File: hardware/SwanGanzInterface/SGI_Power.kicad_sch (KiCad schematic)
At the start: 23 parts, among them IC2 LM2937ET-3.3_NOPB, IC3 LM4041CILPR, J1 2479774-1, Q1 SQ2389CES-T1_GE3, SW1 Power_Switch, U3 OPA2350

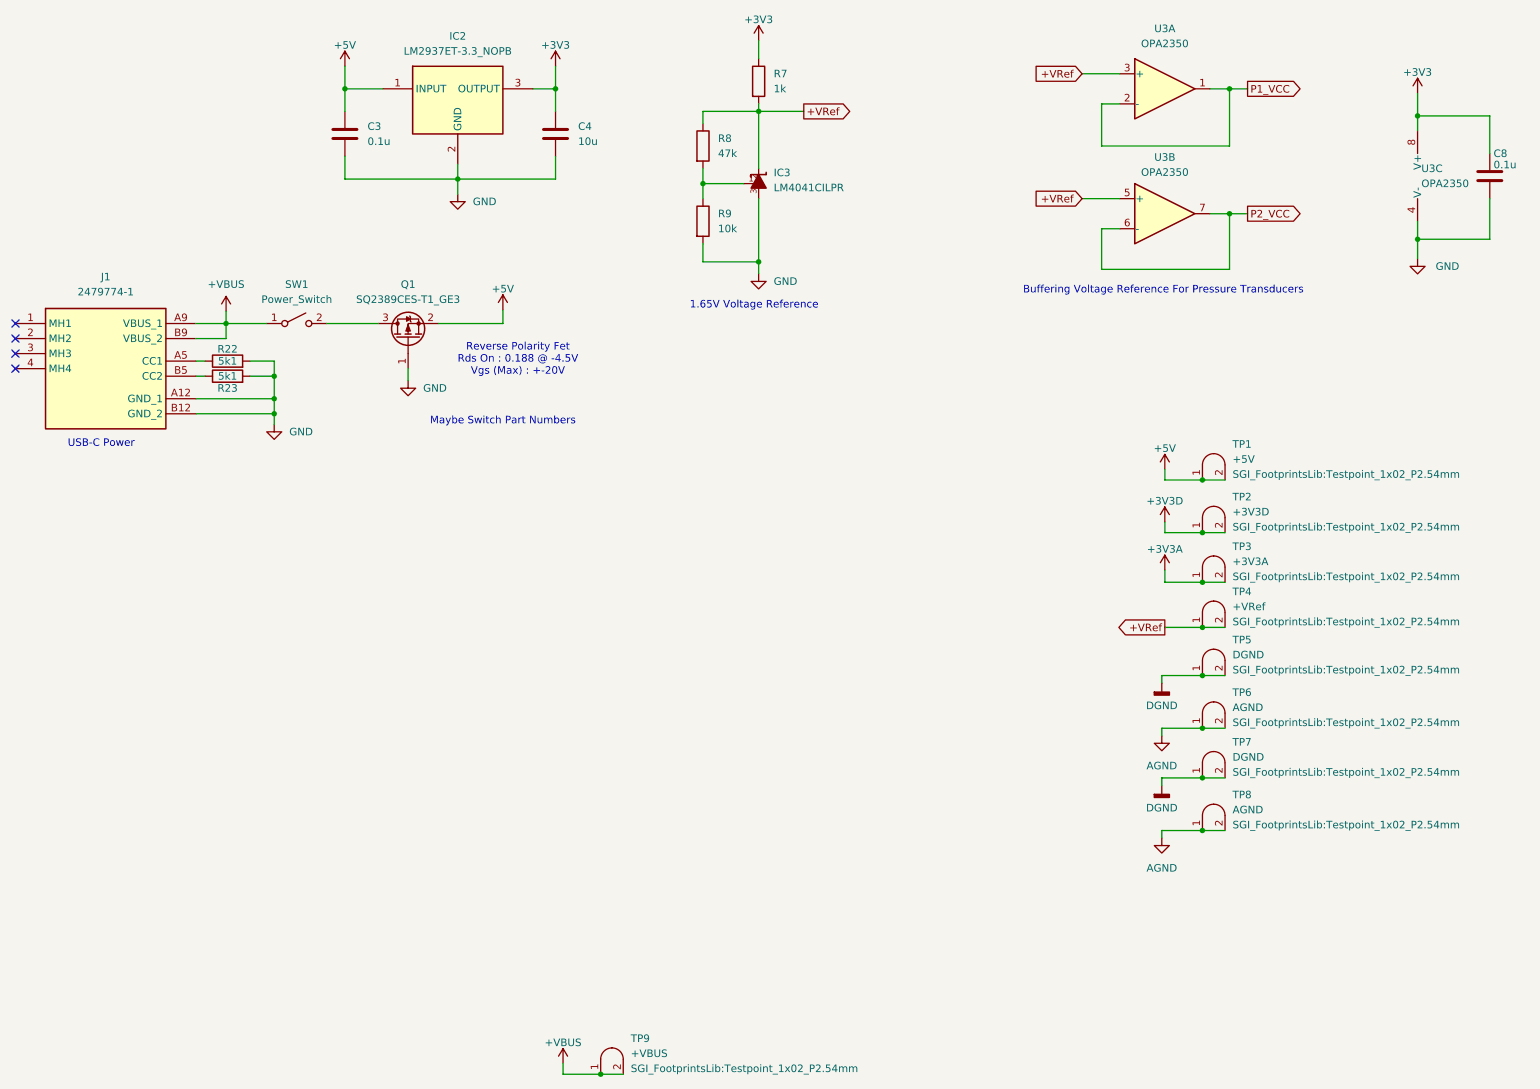
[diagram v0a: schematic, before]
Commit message: Added launchpad, power jumpers, messed with symbol lib
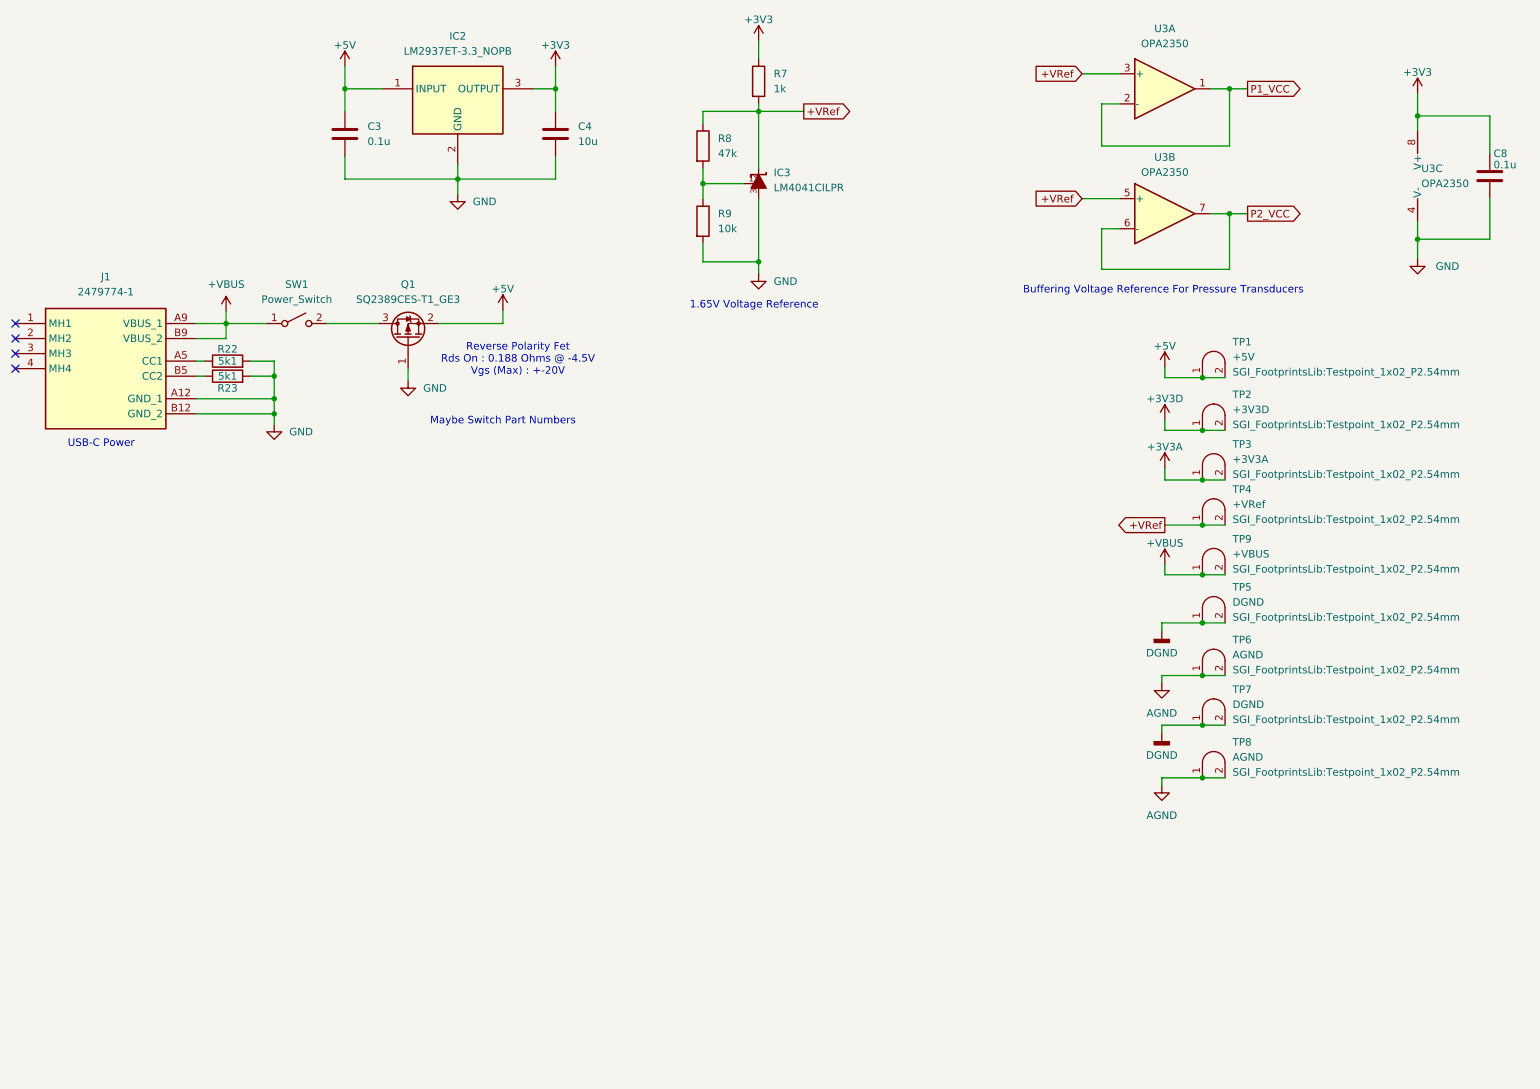
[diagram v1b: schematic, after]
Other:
- note added: "Reverse Polarity Fet Rds On : 0.188 Ohms @ -4.5V Vgs (Max) : +-20V"
- note removed: "Reverse Polarity Fet Rds On : 0.188 @ -4.5V Vgs (Max) : +-20V"
- moved on the sheet: TP1, TP2, TP3, TP4, TP5, TP6, TP7, TP8, TP9

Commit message: Added Test Points to the Outputs of Analog Circuits
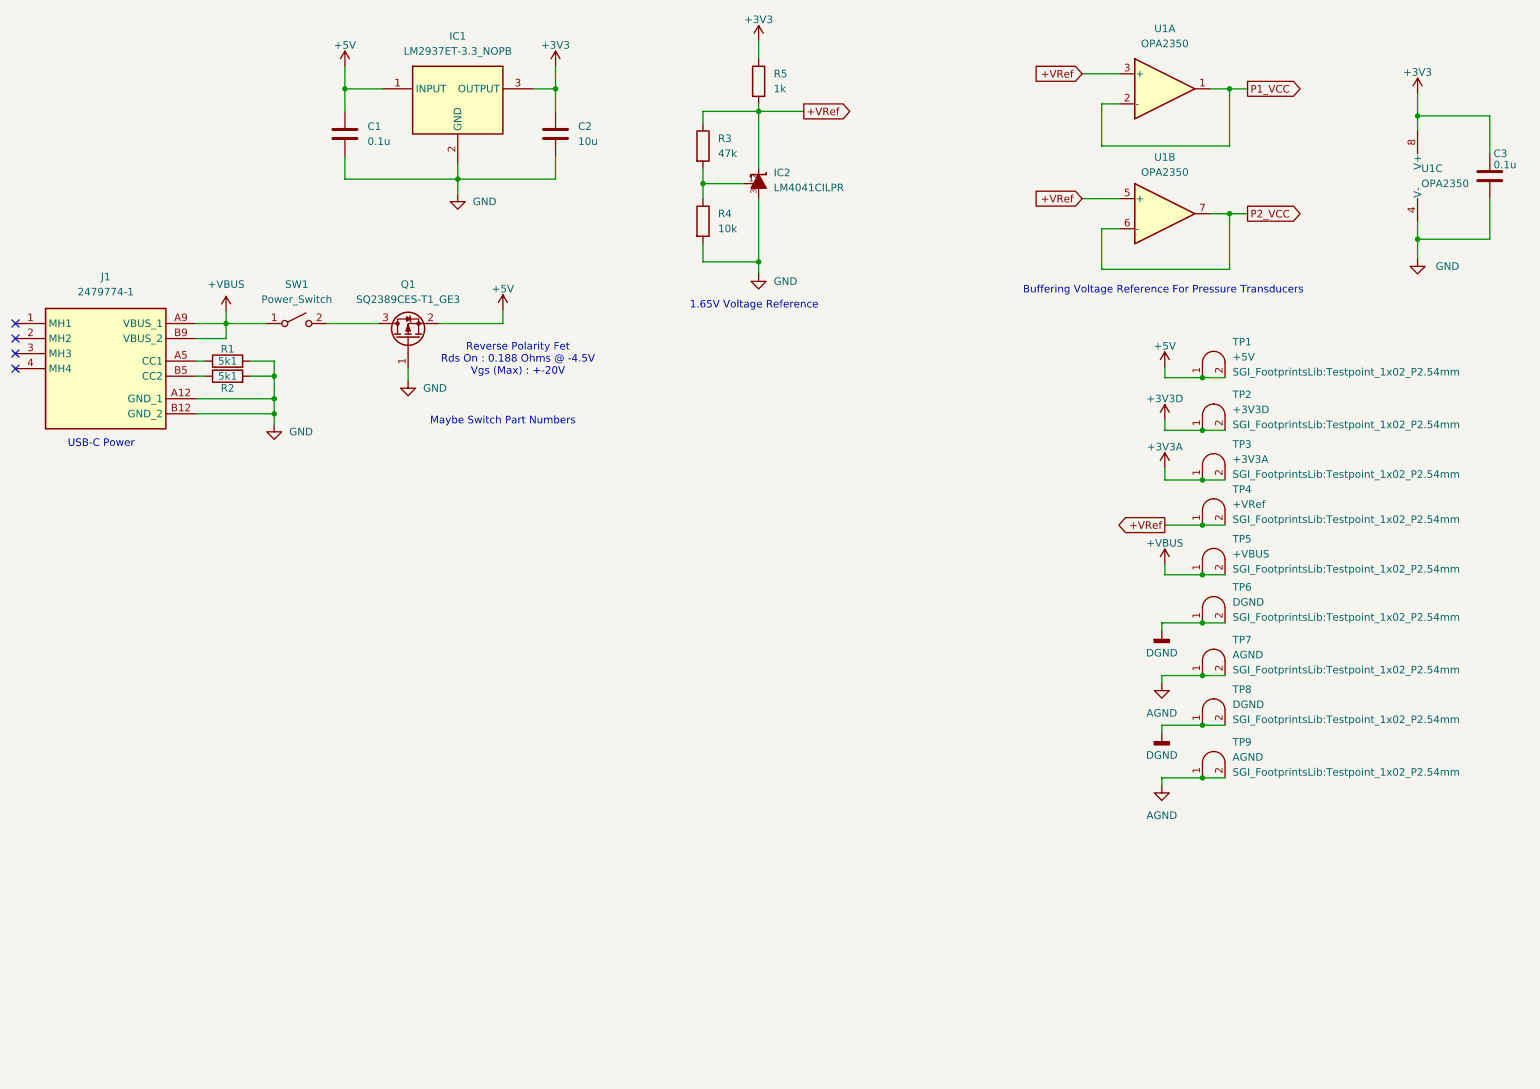
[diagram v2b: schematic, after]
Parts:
- C1: renamed from C3; footprint (none) -> Capacitor_SMD:C_0603_1608Metric
- C2: renamed from C4; footprint (none) -> Capacitor_SMD:C_1206_3216Metric
- C3: renamed from C8; footprint (none) -> Capacitor_SMD:C_0603_1608Metric
- renumbered IC2 to IC1, IC3 to IC2, R22 to R1, R23 to R2, R8 to R3, R9 to R4, R7 to R5, TP9 to TP5, TP5 to TP6, TP6 to TP7, TP7 to TP8, TP8 to TP9, U3 to U1

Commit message: Footprints for most parts, added LCD Driver
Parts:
- R1, R2, R3, R4, R5: footprint (none) -> Resistor_SMD:R_0603_1608Metric
- U2: renamed from IC2; footprint (none) -> SGI_FootprintsLib:ti_LM4041CILPR
- renumbered IC1 to U1, U1 to U3
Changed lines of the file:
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@@
 		(dnp no)
 		(fields_autoplaced yes)
-		(property "Reference" "U1"
+		(property "Reference" "U3"
 			(at 224.79 40.767 0)
 			(effects
@@
 			(project ""
 				(path "/4e9a6e30-f660-472b-9696-bea1f34b4545/090a1e64-9482-4912-b352-6eea35714559"
-					(reference "U1")
+					(reference "U3")
 					(unit 2)
 				)
@@
 		(dnp no)
 		(fields_autoplaced yes)
-		(property "Reference" "IC2"
+		(property "Reference" "U2"
 			(at 158.75 43.3704 0)
 			(effects
@@
 			)
 		)
-		(property "Footprint" ""
+		(property "Footprint" "SGI_FootprintsLib:ti_LM4041CILPR"
 			(at 156.21 45.212 0)
 			(effects
@@
 			(project ""
 				(path "/4e9a6e30-f660-472b-9696-bea1f34b4545/090a1e64-9482-4912-b352-6eea35714559"
-					(reference "IC2")
+					(reference "U2")
 					(unit 1)
 				)
@@
 			)
 		)
-		(property "Footprint" ""
+		(property "Footprint" "Resistor_SMD:R_0603_1608Metric"
 			(at 66.548 79.502 90)
 			(effects
@@
 		(on_board yes)
 		(dnp no)
-		(property "Reference" "U1"
+		(property "Reference" "U3"
 			(at 268.097 42.6719 0)
 			(effects
@@
 			(project ""
 				(path "/4e9a6e30-f660-472b-9696-bea1f34b4545/090a1e64-9482-4912-b352-6eea35714559"
-					(reference "U1")
+					(reference "U3")
 					(unit 3)
 				)
@@
 			)
 		)
-		(property "Footprint" ""
+		(property "Footprint" "Resistor_SMD:R_0603_1608Metric"
 			(at 145.034 38.862 90)
 			(effects
@@
 			)
 		)
-		(property "Footprint" ""
+		(property "Footprint" "Resistor_SMD:R_0603_1608Metric"
 			(at 145.034 51.562 90)
 			(effects
@@
 		(dnp no)
 		(fields_autoplaced yes)
-		(property "Reference" "IC1"
+		(property "Reference" "U1"
 			(at 105.41 20.32 0)
 			(effects
@@
 			(project "SwanGanzInterface"
 				(path "/4e9a6e30-f660-472b-9696-bea1f34b4545/090a1e64-9482-4912-b352-6eea35714559"
-					(reference "IC1")
+					(reference "U1")
 					(unit 1)
 				)
@@
 			)
 		)
-		(property "Footprint" ""
+		(property "Footprint" "Resistor_SMD:R_0603_1608Metric"
 			(at 154.432 27.94 90)
 			(effects
@@
 			)
 		)
-		(property "Footprint" ""
+		(property "Footprint" "Resistor_SMD:R_0603_1608Metric"
 			(at 66.548 76.962 90)
 			(effects
@@
 		(dnp no)
 		(fields_autoplaced yes)
-		(property "Reference" "U1"
+		(property "Reference" "U3"
 			(at 224.79 19.05 0)
 			(effects
@@
 			(project ""
 				(path "/4e9a6e30-f660-472b-9696-bea1f34b4545/090a1e64-9482-4912-b352-6eea35714559"
-					(reference "U1")
-					(unit 1)
-				)
+					(reference "U3")
+					(unit 1)
+				)
